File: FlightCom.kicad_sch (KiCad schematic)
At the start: 52 parts, among them J1 Molex Microfit, J2 Conn_02x03_Counter_Clockwise, U1 TPS62153, U2 W25Q256JVEIQTR, U3 LP5912Q3.3DRVRQ1, U4 USBLC6-2SC6, U5 STM32U575VGTx, X1 1XXD32000MBA

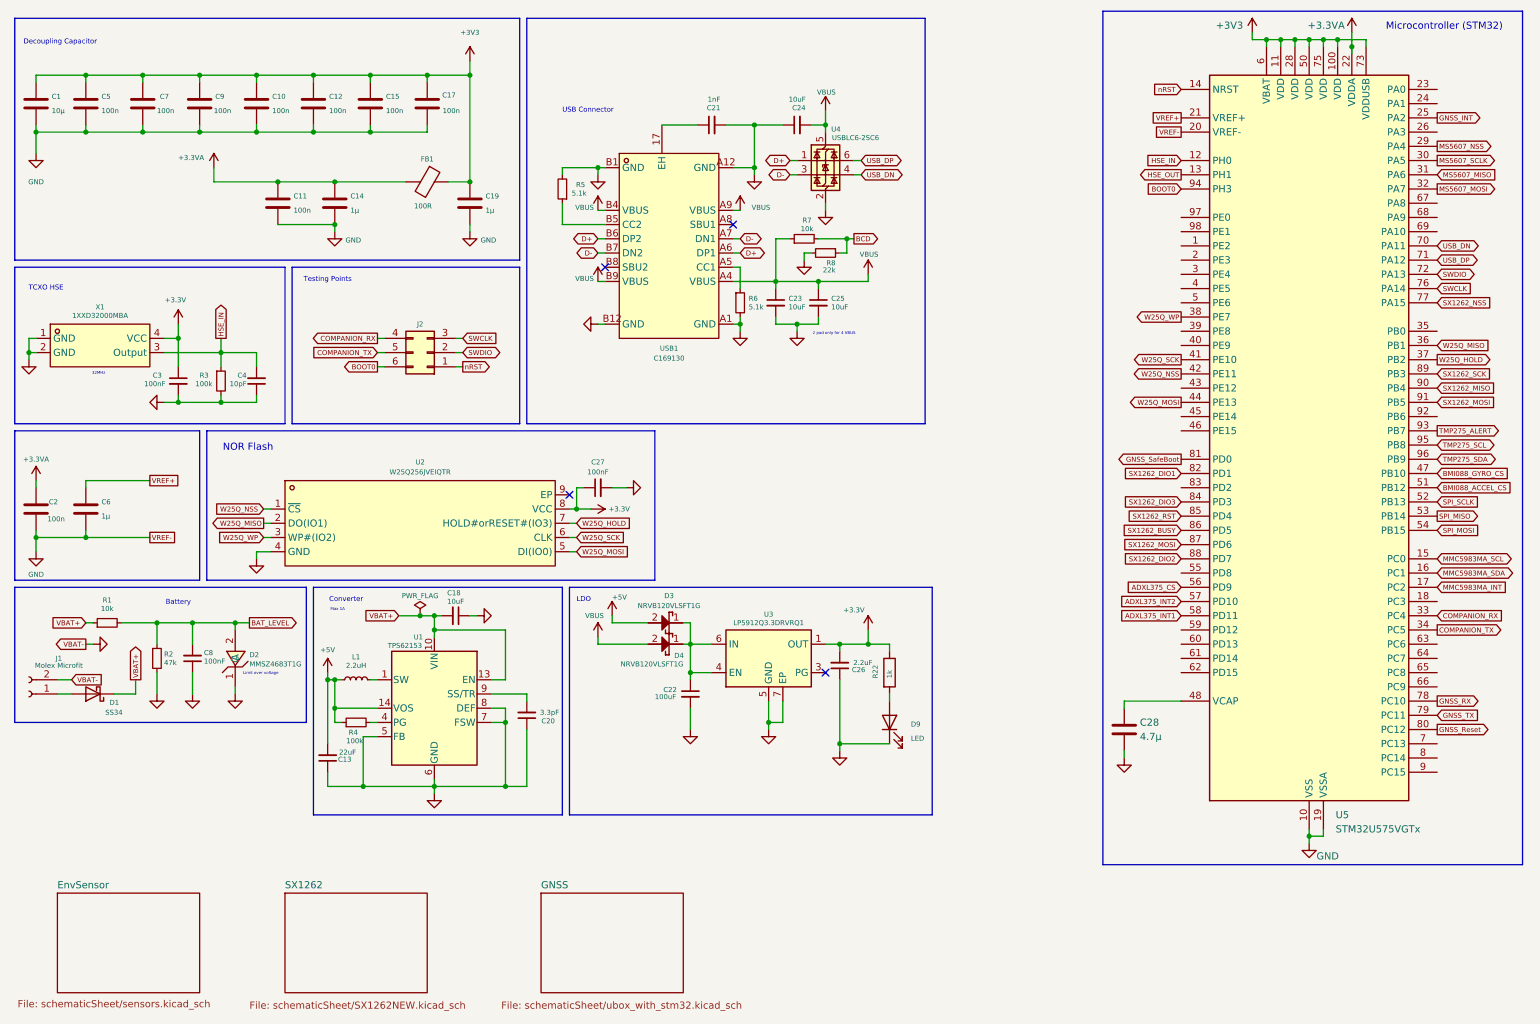
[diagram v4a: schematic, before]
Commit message: add EMMC
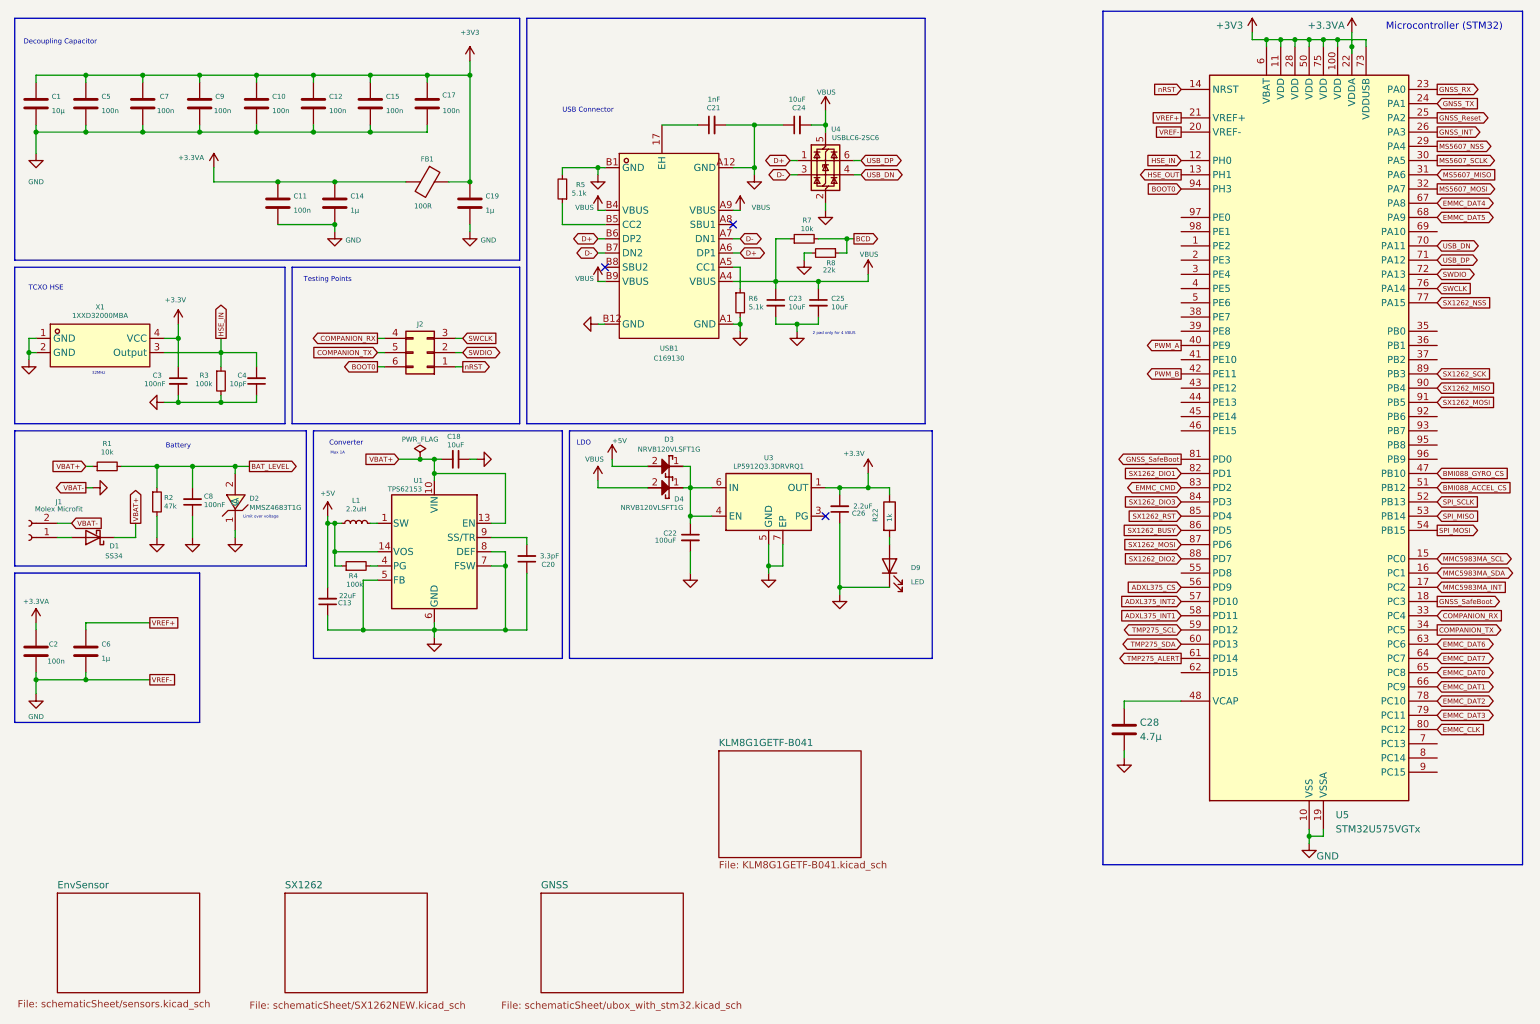
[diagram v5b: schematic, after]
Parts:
- removed C27: 100nF, Capacitor_SMD:C_0402_1005Metric_Pad0.74x0.62mm_HandSolder, symbol Device:C_Small
- removed U2: W25Q256JVEIQTR, EasyEDA:WSON-8_L8.0-W6.10-P1.27-BL-EP, symbol EasyEDA:W25Q256JVEIQTR
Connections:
- net GNSS_INT: now also U5.26 (PA3); no longer U5.25 (PA2)
- net GNSS_RX: now also U5.23 (PA0); no longer U5.78 (PC10)
- net GNSS_Reset: now also U5.25 (PA2); no longer U5.80 (PC12)
- net GNSS_SafeBoot: now also U5.18 (PC3)
- net GNSS_TX: now also U5.24 (PA1); no longer U5.79 (PC11)
- net TMP275_ALERT: now also U5.61 (PD14); no longer U5.93 (PB7)
- net TMP275_SCL: now also U5.59 (PD12); no longer U5.95 (PB8)
- net TMP275_SDA: now also U5.60 (PD13); no longer U5.96 (PB9)
- net PWM_A: now reaches U5.40 (PE9)
- net EMMC_DAT6: now reaches U5.63 (PC6)
- net EMMC_DAT7: now reaches U5.64 (PC7)
- net EMMC_DAT0: now reaches U5.65 (PC8)
- net EMMC_DAT1: now reaches U5.66 (PC9)
- net EMMC_DAT4: now reaches U5.67 (PA8)
- net EMMC_DAT5: now reaches U5.68 (PA9)
- net EMMC_CMD: now reaches U5.83 (PD2)
- net W25Q_HOLD: no longer names the net of U5.37 (PB2)
- net W25Q_MISO: no longer names the net of U5.36 (PB1)
- net W25Q_MOSI: no longer names the net of U5.44 (PE13)
- net W25Q_NSS renamed PWM_B
- net W25Q_SCK: no longer names the net of U5.41 (PE10)
- net W25Q_WP: no longer names the net of U5.38 (PE7)
- new net EMMC_CLK: U5.80 (PC12)
- new net EMMC_DAT2: U5.78 (PC10)
- new net EMMC_DAT3: U5.79 (PC11)
- no-connect marks 4 -> 3
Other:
- added sheet KLM8G1GETF-B041 (KLM8G1GETF-B041.kicad_sch)
- note removed: "NOR Flash"
- moved on the sheet: C13, C18, C2, C20, C22, C26, C6, C8, D1, D2, D3, D4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

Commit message: update schematic
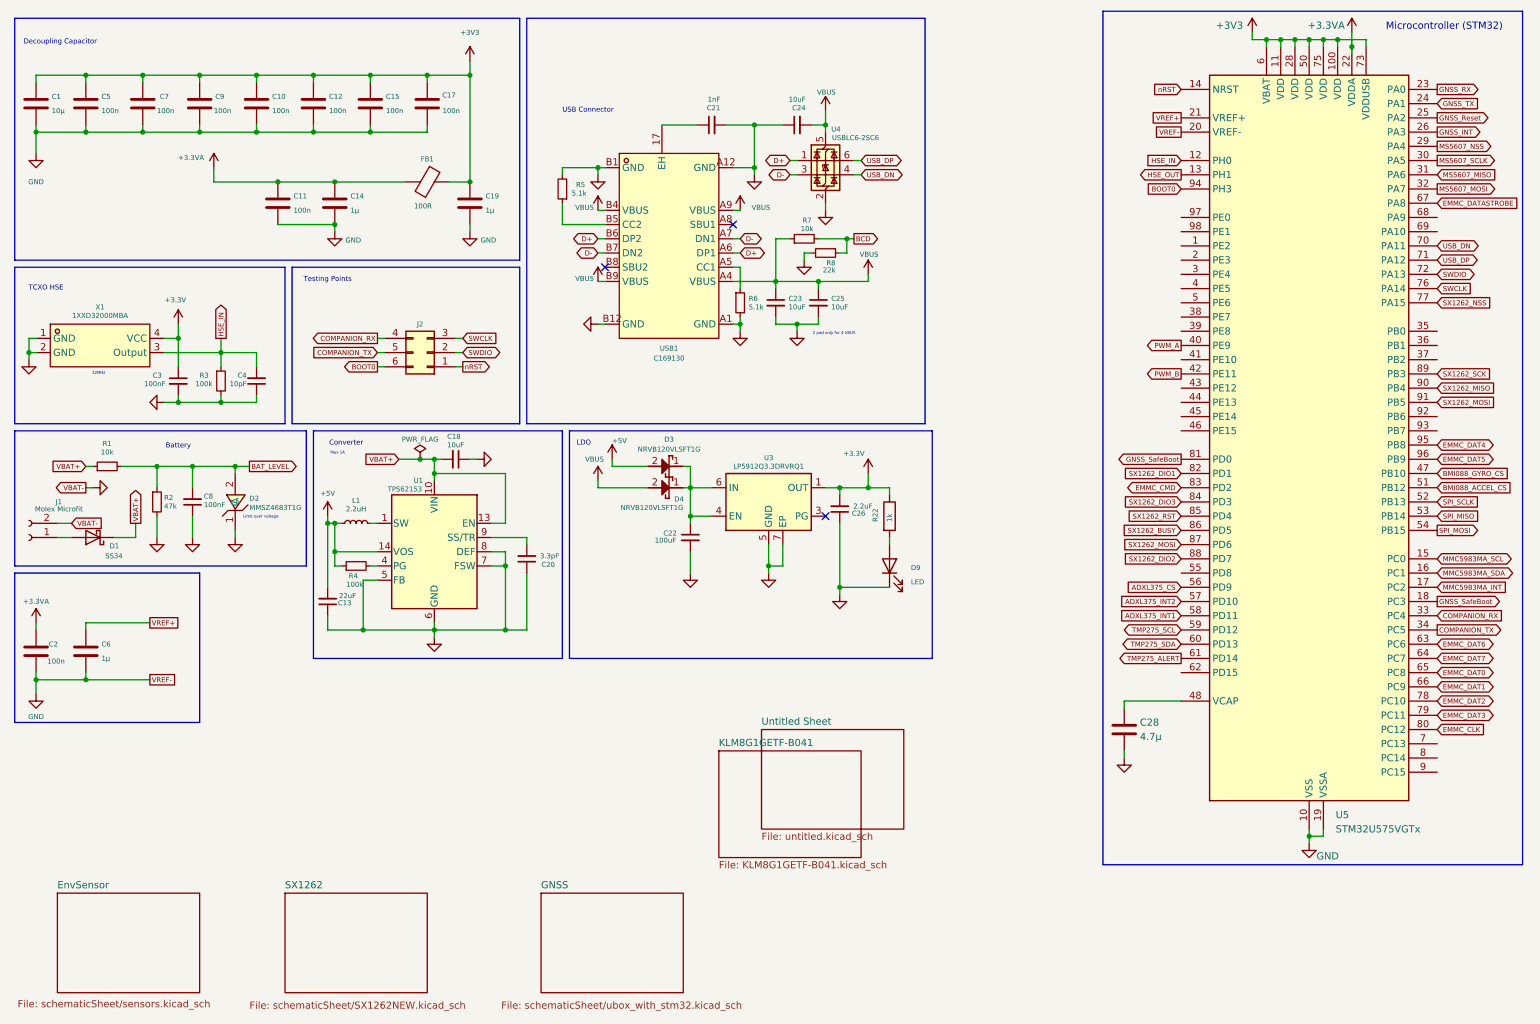
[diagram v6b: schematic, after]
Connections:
- net EMMC_DAT4: now also U5.95 (PB8); no longer U5.67 (PA8)
- net EMMC_DAT5: now also U5.96 (PB9); no longer U5.68 (PA9)
- new net EMMC_DATASTROBE: U5.67 (PA8)
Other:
- added sheet Untitled Sheet (untitled.kicad_sch)
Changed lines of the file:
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@@
 		)
 	)
+	(global_label "EMMC_DATASTROBE"
+		(shape input)
+		(at 269.24 46.99 0)
+		(fields_autoplaced yes)
+		(effects
+			(font
+				(size 0.889 0.889)
+			)
+			(justify left)
+		)
+		(property "Intersheetrefs" "${INTERSHEET_REFS}"
+			(at 283.86 46.99 0)
+			(effects
+				(font
+					(size 1.27 1.27)
+				)
+				(justify left)
+				(hide yes)
+			)
+		)
+	)
 	(global_label "SX1262_RST"
 		(shape input)
@@
 		)
 	)
+	(global_label "EMMC_DAT4"
+		(shape bidirectional)
+		(at 269.24 90.17 0)
+		(fields_autoplaced yes)
+		(effects
+			(font
+				(size 0.889 0.889)
+			)
+			(justify left)
+		)
+		(property "Intersheetrefs" "${INTERSHEET_REFS}"
+			(at 279.685 90.17 0)
+			(effects
+				(font
+					(size 1.27 1.27)
+				)
+				(justify left)
+				(hide yes)
+			)
+		)
+	)
 	(global_label "VBAT-"
 		(shape output)
@@
 		)
 	)
-	(global_label "EMMC_DAT5"
-		(shape bidirectional)
-		(at 269.24 49.53 0)
-		(fields_autoplaced yes)
-		(effects
-			(font
-				(size 0.889 0.889)
-			)
-			(justify left)
-		)
-		(property "Intersheetrefs" "${INTERSHEET_REFS}"
-			(at 279.685 49.53 0)
-			(effects
-				(font
-					(size 1.27 1.27)
-				)
-				(justify left)
-				(hide yes)
-			)
-		)
-	)
 	(global_label "USB_DN"
 		(shape bidirectional)
@@
 		)
 	)
+	(global_label "EMMC_DAT5"
+		(shape bidirectional)
+		(at 269.24 92.71 0)
+		(fields_autoplaced yes)
+		(effects
+			(font
+				(size 0.889 0.889)
+			)
+			(justify left)
+		)
+		(property "Intersheetrefs" "${INTERSHEET_REFS}"
+			(at 279.685 92.71 0)
+			(effects
+				(font
+					(size 1.27 1.27)
+				)
+				(justify left)
+				(hide yes)
+			)
+		)
+	)
 	(global_label "VREF+"
 		(shape passive)
@@
 		)
 	)
-	(global_label "EMMC_DAT4"
-		(shape bidirectional)
-		(at 269.24 46.99 0)
-		(fields_autoplaced yes)
-		(effects
-			(font
-				(size 0.889 0.889)
-			)
-			(justify left)
-		)
-		(property "Intersheetrefs" "${INTERSHEET_REFS}"
-			(at 279.685 46.99 0)
-			(effects
-				(font
-					(size 1.27 1.27)
-				)
-				(justify left)
-				(hide yes)
-			)
-		)
-	)
 	(symbol
 		(lib_id "power:GND")
@@
 				)
 			)
+		)
+	)
+	(sheet
+		(at 148.59 140.97)
+		(size 25.4 17.78)
+		(fields_autoplaced yes)
+		(stroke
+			(width 0.1524)
+			(type solid)
+		)
+		(fill
+			(color 0 0 0 0.0000)
+		)
+		(property "Sheetname" "Untitled Sheet"
+			(at 148.59 140.2584 0)
+			(effects
+				(font
+					(size 1.27 1.27)
+				)
+				(justify left bottom)
+			)
+		)
+		(property "Sheetfile" "untitled.kicad_sch"
+			(at 148.59 159.3346 0)
+			(effects
+				(font
+					(size 1.27 1.27)
+				)
+				(justify left top)
+			)
+		)
+		(instances
+			(project "FlightCom"
+				(path "/f49728bb-5f62-4190-bb7d-54bb4c159a74"
+					(page "5")
+				)
+			)

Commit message: update
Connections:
- net EMMC_RSTN: now reaches U5.68 (PA9)
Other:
- removed sheet Untitled Sheet
- sheet KLM8G1GETF-B041: file KLM8G1GETF-B041.kicad_sch -> schematicSheet/KLM8G1GETF-B041.kicad_sch
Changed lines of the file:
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@@
 		)
 	)
+	(global_label "EMMC_RSTN"
+		(shape output)
+		(at 269.24 49.53 0)
+		(fields_autoplaced yes)
+		(effects
+			(font
+				(size 0.889 0.889)
+			)
+			(justify left)
+		)
+		(property "Intersheetrefs" "${INTERSHEET_REFS}"
+			(at 279.0764 49.53 0)
+			(effects
+				(font
+					(size 1.27 1.27)
+				)
+				(justify left)
+				(hide yes)
+			)
+		)
+	)
 	(global_label "SX1262_MOSI"
 		(shape input)
@@
 	)
 	(sheet
-		(at 63.5 170.18)
+		(at 58.42 170.18)
 		(size 25.4 17.78)
 		(stroke
@@
 		)
 		(property "Sheetname" "SX1262"
-			(at 63.5 169.4684 0)
+			(at 58.42 169.4684 0)
 			(effects
 				(font
@@
 		)
 		(property "Sheetfile" "schematicSheet/SX1262NEW.kicad_sch"
-			(at 57.15 189.484 0)
+			(at 55.88 189.738 0)
 			(effects
 				(font
-					(size 1.27 1.27)
+					(size 0.889 0.889)
 				)
 				(justify left top)
@@
 	)
 	(sheet
-		(at 109.22 170.18)
+		(at 93.98 170.18)
 		(size 25.4 17.78)
 		(stroke
@@
 		)
 		(property "Sheetname" "GNSS"
-			(at 109.22 169.4684 0)
+			(at 93.98 169.4684 0)
 			(effects
 				(font
@@
 		)
 		(property "Sheetfile" "schematicSheet/ubox_with_stm32.kicad_sch"
-			(at 102.108 189.484 0)
+			(at 91.186 189.738 0)
 			(effects
 				(font
-					(size 1.27 1.27)
+					(size 0.889 0.889)
 				)
 				(justify left top)
@@
 	)
 	(sheet
-		(at 148.59 140.97)
-		(size 25.4 17.78)
-		(fields_autoplaced yes)
-		(stroke
-			(width 0.1524)
-			(type solid)
-		)
-		(fill
-			(color 0 0 0 0.0000)
-		)
-		(property "Sheetname" "Untitled Sheet"
-			(at 148.59 140.2584 0)
-			(effects
-				(font
-					(size 1.27 1.27)
-				)
-				(justify left bottom)
-			)
-		)
-		(property "Sheetfile" "untitled.kicad_sch"
-			(at 148.59 159.3346 0)
-			(effects
-				(font
-					(size 1.27 1.27)
-				)
-				(justify left top)
-			)
-		)
-		(instances
-			(project "FlightCom"
-				(path "/f49728bb-5f62-4190-bb7d-54bb4c159a74"
-					(page "5")
-				)
-			)
-		)
-	)
-	(sheet
-		(at 140.97 144.78)
+		(at 135.89 168.91)
 		(size 25.4 19.05)
-		(fields_autoplaced yes)
 		(stroke
 			(width 0.1524)
@@
 		)
 		(property "Sheetname" "KLM8G1GETF-B041"
-			(at 140.97 144.0684 0)
+			(at 135.89 168.1984 0)
 			(effects
 				(font
@@
 			)
 		)
-		(property "Sheetfile" "KLM8G1GETF-B041.kicad_sch"
-			(at 140.97 164.4146 0)
+		(property "Sheetfile" "schematicSheet/KLM8G1GETF-B041.kicad_sch"
+			(at 132.08 189.738 0)
 			(effects
 				(font
-					(size 1.27 1.27)
+					(size 0.889 0.889)
 				)
 				(justify left top)
@@
 		)
 		(property "Sheetfile" "schematicSheet/sensors.kicad_sch"
-			(at 15.748 189.23 0)
+			(at 21.59 189.23 0)
 			(effects
 				(font
-					(size 1.27 1.27)
+					(size 0.889 0.889)
 				)
 				(justify left top)

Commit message: update
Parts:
- D9: footprint LED_SMD:LED_0805_2012Metric -> LED_SMD:LED_0402_1005Metric
- R22: footprint Resistor_SMD:R_0805_2012Metric -> Resistor_SMD:R_0402_1005Metric
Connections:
- net +3V3 is gone; now on net +3.3V: C1.1, C10.1, C12.1, C15.1, C17.2, C19.1, C5.1, C7.1, C9.1, FB1.1, U5.100 (VDD), U5.11 (VDD), U5.28 (VDD), U5.50 (VDD), U5.6 (VBAT), U5.73 (VDDUSB), U5.75 (VDD)
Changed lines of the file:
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@@
 			)
 		)
-		(property "Footprint" "LED_SMD:LED_0805_2012Metric"
+		(property "Footprint" "LED_SMD:LED_0402_1005Metric"
 			(at 171.45 111.76 0)
 			(effects
@@
 			)
 		)
-		(property "Value" "+3V3"
+		(property "Value" "+3.3V"
 			(at 232.156 15.24 0)
 			(effects
@@
 			)
 		)
-		(property "Value" "+3V3"
+		(property "Value" "+3.3V"
 			(at 96.52 16.51 0)
 			(effects
@@
 			)
 		)
-		(property "Footprint" "Resistor_SMD:R_0805_2012Metric"
+		(property "Footprint" "Resistor_SMD:R_0402_1005Metric"
 			(at 169.672 102.87 90)
 			(effects
@@
 		)
 		(property "Value" "100k"
-			(at 75.946 115.062 90)
+			(at 76.2 111.76 90)
 			(effects
 				(font
